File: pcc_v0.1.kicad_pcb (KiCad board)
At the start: 2 copper layers, 190.3 x 121.7 mm, 60 parts, among them J1 Conn_01x02_Socket, J2 Conn_01x04_Socket, J3 Conn_01x02_Socket, J4 Conn_02x14_Counter_Clockwise, J5 Conn_01x06_Socket, J7 Conn_01x04_Socket, J8 Conn_01x02_Socket, J9 Conn_01x02_Socket, K1 G9KB-1A_DC12, K3 PCN-112D3MHZ_000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

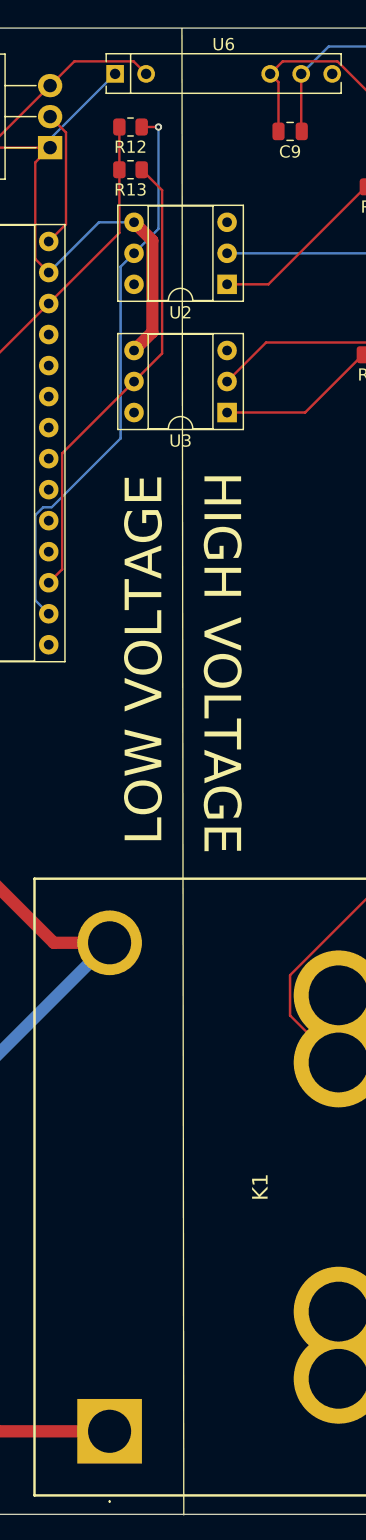
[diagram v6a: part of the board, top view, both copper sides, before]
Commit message: next round of changes with correct precharge resistor and isolation distance
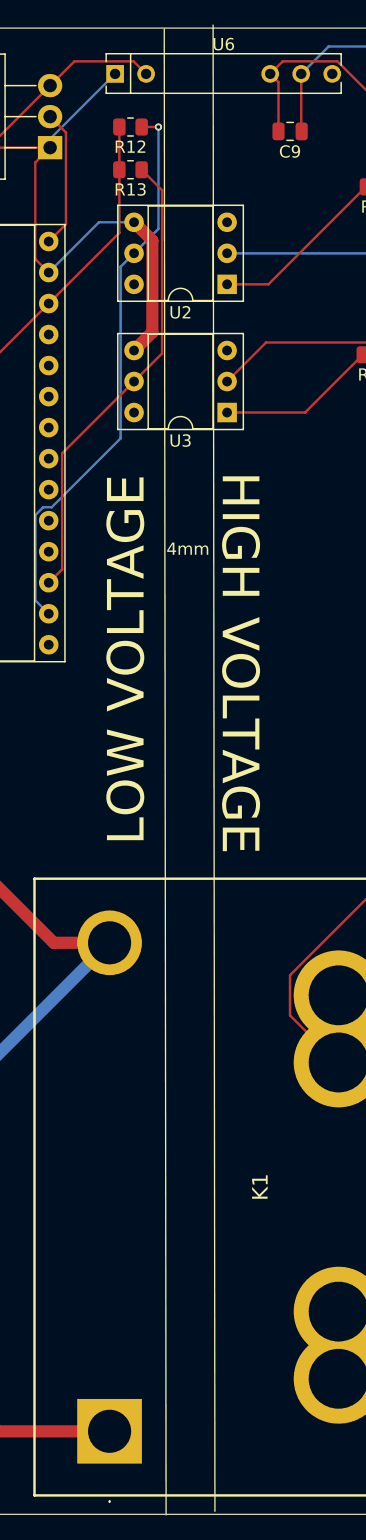
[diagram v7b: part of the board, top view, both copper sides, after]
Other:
- board text added: "4mm"
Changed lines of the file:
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@@
 		(tags "connector Molex Mini-Fit_Jr side entryplastic_peg")
 		(property "Reference" "J9"
-			(at 0 -3.45 360)
+			(at 0 -3.45 0)
 			(layer "F.SilkS")
 			(effects
@@
 		)
 		(property "Value" "Conn_01x02_Socket"
-			(at 0 9.95 360)
+			(at 0 9.95 0)
 			(layer "F.Fab")
 			(effects
@@
 		)
 		(fp_text user "${REFERENCE}"
-			(at 0 -1.55 360)
+			(at 0 -1.55 0)
 			(layer "F.Fab")
 			(effects
@@
 		)
 		(property "Footprint" "PCN_112D3HMZ:RELAY_PCN-105D3MHZ_000_TEC"
-			(at 0 0 360)
+			(at 0 0 0)
 			(layer "F.Fab")
 			(hide yes)
@@
 		)
 		(property "Datasheet" "PCN-112D3MHZ_000"
-			(at 0 0 360)
+			(at 0 0 0)
 			(layer "F.Fab")
 			(hide yes)
@@
 		)
 		(property "Description" ""
-			(at 0 0 360)
+			(at 0 0 0)
 			(layer "F.Fab")
 			(hide yes)
@@
 		(tags "connector Molex Mini-Fit_Jr side entryplastic_peg")
 		(property "Reference" "J5"
-			(at 4.2 -3.45 360)
+			(at 4.2 -3.45 0)
 			(layer "F.SilkS")
 			(effects
@@
 		)
 		(property "Value" "Conn_01x06_Socket"
-			(at 3.549747 11.450253 360)
+			(at 3.549747 11.450253 0)
 			(layer "F.Fab")
 			(effects
@@
 		)
 		(fp_text user "${REFERENCE}"
-			(at 4.2 -1.55 360)
+			(at 4.2 -1.55 0)
 			(layer "F.Fab")
 			(effects
@@
 		)
 		(property "Footprint" "nmos:SOIC_63D8L-7_DIO"
-			(at 0 0 360)
+			(at 0 0 0)
 			(layer "F.Fab")
 			(hide yes)
@@
 		)
 		(property "Datasheet" "DMN63D8L-7"
-			(at 0 0 360)
+			(at 0 0 0)
 			(layer "F.Fab")
 			(hide yes)
@@
 		)
 		(property "Description" ""
-			(at 0 0 360)
+			(at 0 0 0)
 			(layer "F.Fab")
 			(hide yes)
@@
 		(tags "resistor")
 		(property "Reference" "R27"
-			(at 0 -1.65 360)
+			(at 0 -1.65 0)
 			(layer "F.SilkS")
 			(effects
@@
 		)
 		(property "Value" "120"
-			(at 0 1.65 360)
+			(at 0 1.65 0)
 			(layer "F.Fab")
 			(effects
@@
 		)
 		(fp_text user "${REFERENCE}"
-			(at 0 0 360)
+			(at 0 0 0)
 			(layer "F.Fab")
 			(effects
@@
 	)
 	(gr_line
-		(start 101.874873 30.799873)
-		(end 102.025126 152.500126)
+		(start 100.424873 30.799873)
+		(end 100.575126 152.500126)
+		(stroke
+			(width 0.1)
+			(type default)
+		)
+		(layer "F.SilkS")
+	)
+	(gr_line
+		(start 104.424873 30.5)
+		(end 104.575126 152.200253)
 		(stroke
 			(width 0.1)
@@
 		(layer "Edge.Cuts")
 	)
+	(gr_text "4mm"
+		(at 100.6 74 0)
+		(layer "F.SilkS")
+		(effects
+			(font
+				(size 1 1)
+				(thickness 0.1)
+			)
+			(justify left bottom)
+		)
+	)
 	(gr_text "HIGH VOLTAGE\n"
-		(at 103.35 67.05 -90)
+		(at 104.85 67.05 -90)
 		(layer "F.SilkS")
 		(effects
@@
 	)
 	(gr_text "LOW VOLTAGE"
-		(at 100.55 97.65 90)
+		(at 99.1 97.65 90)
 		(layer "F.SilkS")
 		(effects

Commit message: next round of edits
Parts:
- removed J5: Conn_01x06_Socket, Connector_Molex:Molex_Mini-Fit_Jr_5566-06A2_2x03_P4.20mm_Vertical
- added J6: Conn_01x04_Socket, Connector_Molex:Molex_Mini-Fit_Jr_5566-04A2_2x02_P4.20mm_Vertical, F.Cu at (209.2, 41.1)
- moved R29 99.6 mm to (240.7, 49.0), turned to 180 degrees
- moved C8 0.21 mm to (141.8, 63.2)
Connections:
- R21 pad 1: B+_out -> GNDS
- R28 pad 1: B+_out -> GNDS
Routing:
- net B+_out: track 165.8 -> 0.00 mm, vias 1 -> 0
- net GNDS: track 243.2 -> 372.2 mm, vias 4 -> 2
- net Vin_Accu: track 191.1 -> 104.4 mm
- net Net-(R28-Pad2): track 100.8 -> 52.9 mm
- net B+_in: track 159.3 -> 140.7 mm
- net TS+: track 22.1 -> 16.7 mm
- net +12P: track 136.0 -> 131.4 mm, vias 0 -> 1
- net TS-: track 26.5 -> 22.0 mm
- added copper zone on B.Cu, net GLV-
